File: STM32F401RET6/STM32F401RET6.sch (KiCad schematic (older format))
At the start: 12 parts

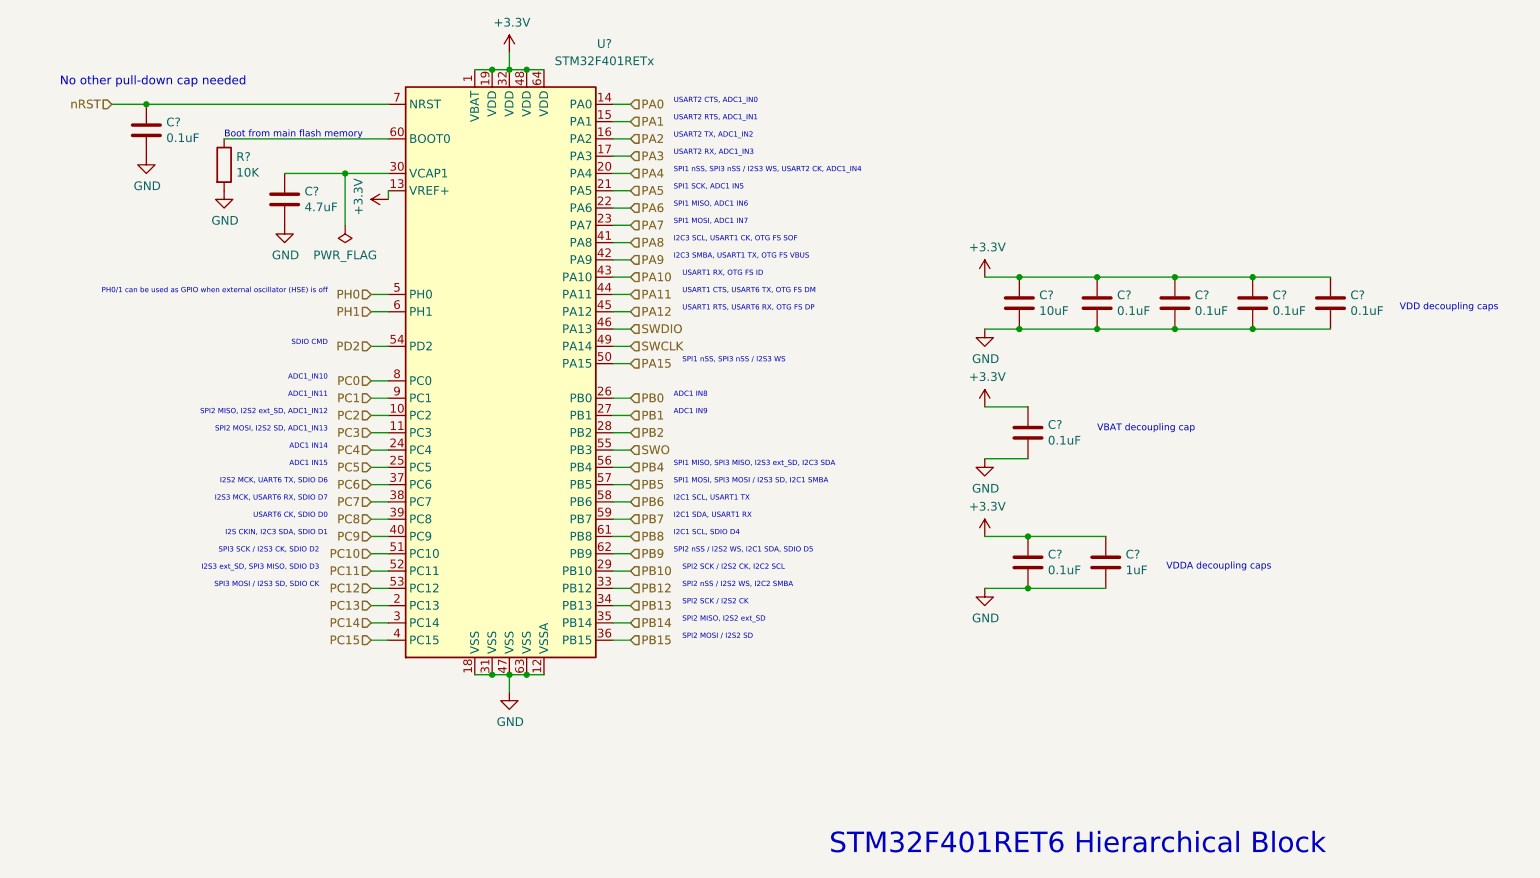
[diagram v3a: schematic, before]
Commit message: add symbol libraries, and cleanup
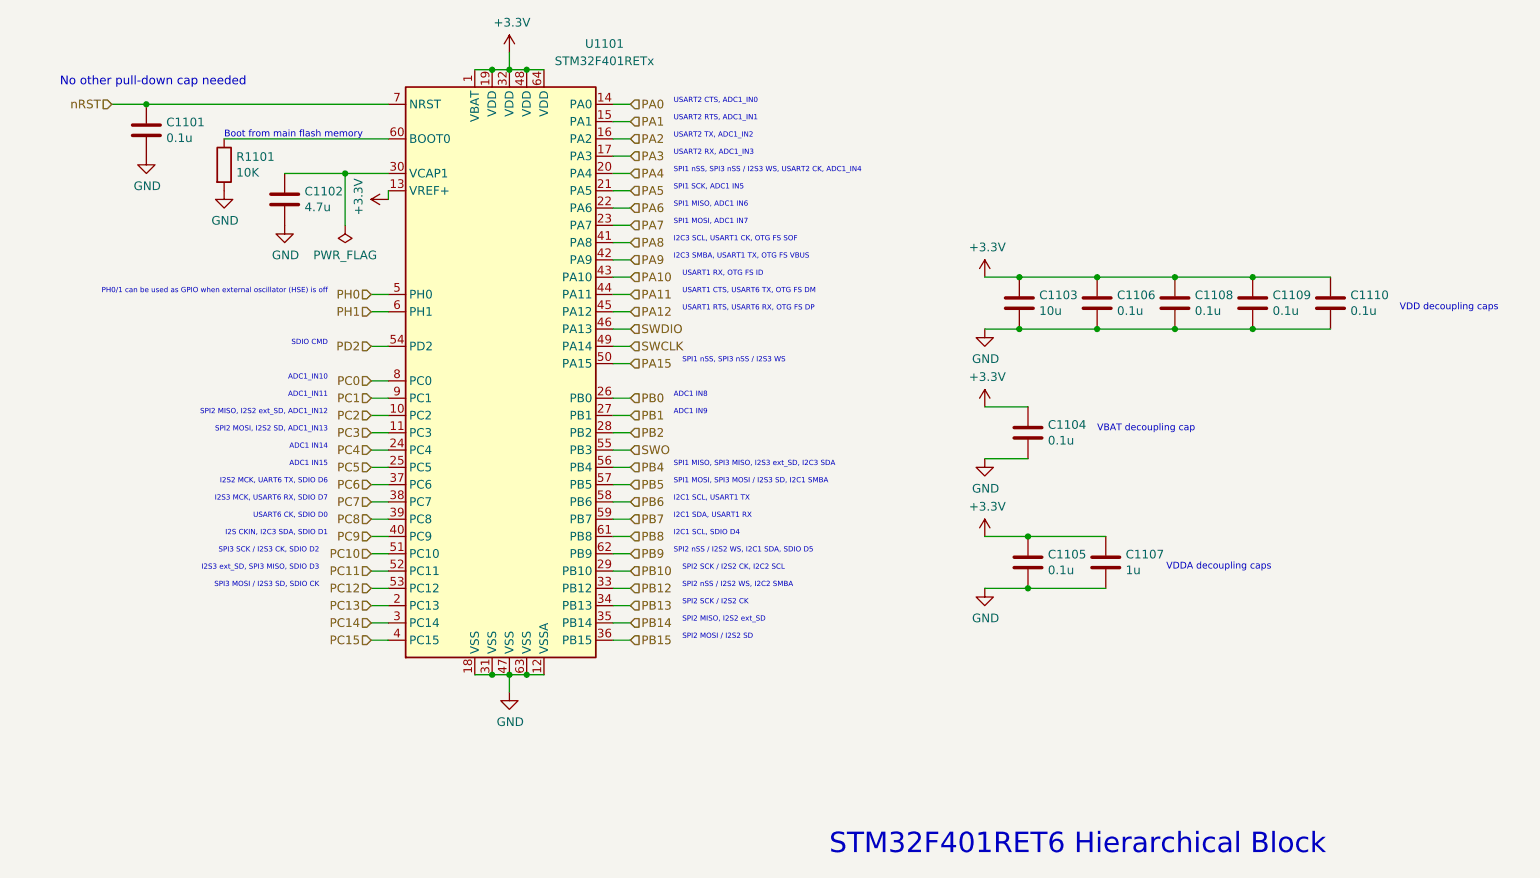
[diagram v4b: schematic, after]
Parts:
- C1101, C1104, C1105, C1106, C1108, C1109, C1110: renamed from C?; value 0.1uF -> 0.1u; footprint (none) -> Capacitor_SMD:C_0603_1608Metric; DIGIKEY (none) -> 399-1100-1-ND; MANF (none) -> C0603C104Z3VACTU
- C1102: renamed from C?; value 4.7uF -> 4.7u; footprint (none) -> Capacitor_SMD:C_0603_1608Metric; DIGIKEY (none) -> 311-1820-1-ND; MANF (none) -> CC0603MRX5R6BB475
- C1103: renamed from C?; value 10uF -> 10u; footprint (none) -> Capacitor_SMD:C_0603_1608Metric; DIGIKEY (none) -> 490-13248-1-ND; MANF (none) -> GRM188R6YA106MA73D
- C1107: renamed from C?; value 1uF -> 1u; footprint (none) -> Capacitor_SMD:C_0603_1608Metric; DIGIKEY (none) -> 1276-1182-1-ND; MANF (none) -> CL10A105KP8NNNC
- R1101: renamed from R?; footprint (none) -> Resistor_SMD:R_0603_1608Metric; DIGIKEY (none) -> 311-10KGRCT-ND; MANF (none) -> RC0603JR-0710KL
- U1101: renamed from U?; DIGIKEY (none) -> 497-17429-ND; MANF (none) -> STM32F401RET6
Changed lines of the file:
@@
 $Descr A4 11693 8268
 encoding utf-8
-Sheet 4 6
+Sheet 1 1
 Title ""
 Date ""
@@
 $EndDescr
 $Comp
-L MCU_ST_STM32F4:STM32F401RETx U?
+L MCU_ST_STM32F4:STM32F401RETx U1101
 U 1 1 5DE1731E
 P 5250 4100
-F 0 "U?" H 5800 5950 50  0000 C CNN
+F 0 "U1101" H 5800 5950 50  0000 C CNN
 F 1 "STM32F401RETx" H 5800 5850 50  0000 C CNN
 F 2 "Package_QFP:LQFP-64_10x10mm_P0.5mm" H 4650 2400 50  0001 R CNN
 F 3 "http://www.st.com/st-web-ui/static/active/en/resource/technical/document/datasheet/DM00102166.pdf" H 5250 4100 50  0001 C CNN
+F 4 "497-17429-ND" H 5250 4100 50  0001 C CNN "DIGIKEY"
+F 5 "STM32F401RET6" H 5250 4100 50  0001 C CNN "MANF"
 	1    5250 4100
 	1    0    0    -1
@@
 	5250 2300 5250 2400
 $Comp
-L power:GND #PWR?
+L power:GND #PWR01106
 U 1 1 5DE18883
 P 5250 6000
-F 0 "#PWR?" H 5250 5750 50  0001 C CNN
+F 0 "#PWR01106" H 5250 5750 50  0001 C CNN
 F 1 "GND" H 5255 5827 50  0000 C CNN
 F 2 "" H 5250 6000 50  0001 C CNN
@@
 	5250 6000 5250 5900
 $Comp
-L Device:C C?
+L Device:C C1106
 U 1 1 5DE19367
 P 8650 3750
-F 0 "C?" H 8765 3796 50  0000 L CNN
-F 1 "0.1uF" H 8765 3705 50  0000 L CNN
-F 2 "" H 8688 3600 50  0001 C CNN
+F 0 "C1106" H 8765 3796 50  0000 L CNN
+F 1 "0.1u" H 8765 3705 50  0000 L CNN
+F 2 "Capacitor_SMD:C_0603_1608Metric" H 8688 3600 50  0001 C CNN
 F 3 "~" H 8650 3750 50  0001 C CNN
+F 4 "399-1100-1-ND" H 8650 3750 50  0001 C CNN "DIGIKEY"
+F 5 "C0603C104Z3VACTU" H 8650 3750 50  0001 C CNN "MANF"
 	1    8650 3750
 	1    0    0    -1
 $EndComp
 $Comp
-L Device:C C?
+L Device:C C1108
 U 1 1 5DE19787
 P 9100 3750
-F 0 "C?" H 9215 3796 50  0000 L CNN
-F 1 "0.1uF" H 9215 3705 50  0000 L CNN
-F 2 "" H 9138 3600 50  0001 C CNN
+F 0 "C1108" H 9215 3796 50  0000 L CNN
+F 1 "0.1u" H 9215 3705 50  0000 L CNN
+F 2 "Capacitor_SMD:C_0603_1608Metric" H 9138 3600 50  0001 C CNN
 F 3 "~" H 9100 3750 50  0001 C CNN
+F 4 "399-1100-1-ND" H 9100 3750 50  0001 C CNN "DIGIKEY"
+F 5 "C0603C104Z3VACTU" H 9100 3750 50  0001 C CNN "MANF"
 	1    9100 3750
 	1    0    0    -1
 $EndComp
 $Comp
-L Device:C C?
+L Device:C C1109
 U 1 1 5DE19D37
 P 9550 3750
-F 0 "C?" H 9665 3796 50  0000 L CNN
-F 1 "0.1uF" H 9665 3705 50  0000 L CNN
-F 2 "" H 9588 3600 50  0001 C CNN
+F 0 "C1109" H 9665 3796 50  0000 L CNN
+F 1 "0.1u" H 9665 3705 50  0000 L CNN
+F 2 "Capacitor_SMD:C_0603_1608Metric" H 9588 3600 50  0001 C CNN
 F 3 "~" H 9550 3750 50  0001 C CNN
+F 4 "399-1100-1-ND" H 9550 3750 50  0001 C CNN "DIGIKEY"
+F 5 "C0603C104Z3VACTU" H 9550 3750 50  0001 C CNN "MANF"
 	1    9550 3750
 	1    0    0    -1
 $EndComp
 $Comp
-L Device:C C?
+L Device:C C1110
 U 1 1 5DE19F0D
 P 10000 3750
-F 0 "C?" H 10115 3796 50  0000 L CNN
-F 1 "0.1uF" H 10115 3705 50  0000 L CNN
-F 2 "" H 10038 3600 50  0001 C CNN
+F 0 "C1110" H 10115 3796 50  0000 L CNN
+F 1 "0.1u" H 10115 3705 50  0000 L CNN
+F 2 "Capacitor_SMD:C_0603_1608Metric" H 10038 3600 50  0001 C CNN
 F 3 "~" H 10000 3750 50  0001 C CNN
+F 4 "399-1100-1-ND" H 10000 3750 50  0001 C CNN "DIGIKEY"
+F 5 "C0603C104Z3VACTU" H 10000 3750 50  0001 C CNN "MANF"
 	1    10000 3750
 	1    0    0    -1
@@
 	8200 3900 8650 3900
 $Comp
-L Device:C C?
+L Device:C C1103
 U 1 1 5DE19136
 P 8200 3750
-F 0 "C?" H 8315 3796 50  0000 L CNN
-F 1 "10uF" H 8315 3705 50  0000 L CNN
-F 2 "" H 8238 3600 50  0001 C CNN
+F 0 "C1103" H 8315 3796 50  0000 L CNN
+F 1 "10u" H 8315 3705 50  0000 L CNN
+F 2 "Capacitor_SMD:C_0603_1608Metric" H 8238 3600 50  0001 C CNN
 F 3 "~" H 8200 3750 50  0001 C CNN
+F 4 "490-13248-1-ND" H 8200 3750 50  0001 C CNN "DIGIKEY"
+F 5 "GRM188R6YA106MA73D" H 8200 3750 50  0001 C CNN "MANF"
 	1    8200 3750
 	1    0    0    -1
 $EndComp
 $Comp
-L power:GND #PWR?
+L power:GND #PWR01108
 U 1 1 5DE18B06
 P 8000 3900
-F 0 "#PWR?" H 8000 3650 50  0001 C CNN
+F 0 "#PWR01108" H 8000 3650 50  0001 C CNN
 F 1 "GND" H 8005 3727 50  0000 C CNN
 F 2 "" H 8000 3900 50  0001 C CNN
@@
 $EndComp
 $Comp
-L power:GND #PWR?
+L power:GND #PWR01110
 U 1 1 5DE1D921
 P 8000 4650
-F 0 "#PWR?" H 8000 4400 50  0001 C CNN
+F 0 "#PWR01110" H 8000 4400 50  0001 C CNN
 F 1 "GND" H 8005 4477 50  0000 C CNN
 F 2 "" H 8000 4650 50  0001 C CNN
@@
 $EndComp
 $Comp
-L Device:C C?
+L Device:C C1104
 U 1 1 5DE1DB7A
 P 8250 4500
-F 0 "C?" H 8365 4546 50  0000 L CNN
-F 1 "0.1uF" H 8365 4455 50  0000 L CNN
-F 2 "" H 8288 4350 50  0001 C CNN
+F 0 "C1104" H 8365 4546 50  0000 L CNN
+F 1 "0.1u" H 8365 4455 50  0000 L CNN
+F 2 "Capacitor_SMD:C_0603_1608Metric" H 8288 4350 50  0001 C CNN
 F 3 "~" H 8250 4500 50  0001 C CNN
+F 4 "399-1100-1-ND" H 8250 4500 50  0001 C CNN "DIGIKEY"
+F 5 "C0603C104Z3VACTU" H 8250 4500 50  0001 C CNN "MANF"
 	1    8250 4500
 	1    0    0    -1
@@
 	8250 4350 8000 4350
 $Comp
-L Device:C C?
+L Device:C C1105
 U 1 1 5DE1EBB5
 P 8250 5250
-F 0 "C?" H 8365 5296 50  0000 L CNN
-F 1 "0.1uF" H 8365 5205 50  0000 L CNN
-F 2 "" H 8288 5100 50  0001 C CNN
+F 0 "C1105" H 8365 5296 50  0000 L CNN
+F 1 "0.1u" H 8365 5205 50  0000 L CNN
+F 2 "Capacitor_SMD:C_0603_1608Metric" H 8288 5100 50  0001 C CNN
 F 3 "~" H 8250 5250 50  0001 C CNN
+F 4 "399-1100-1-ND" H 8250 5250 50  0001 C CNN "DIGIKEY"
+F 5 "C0603C104Z3VACTU" H 8250 5250 50  0001 C CNN "MANF"
 	1    8250 5250
 	1    0    0    -1
 $EndComp
 $Comp
-L power:GND #PWR?
+L power:GND #PWR01112
 U 1 1 5DE1F4FA
 P 8000 5400
-F 0 "#PWR?" H 8000 5150 50  0001 C CNN
+F 0 "#PWR01112" H 8000 5150 50  0001 C CNN
 F 1 "GND" H 8005 5227 50  0000 C CNN
 F 2 "" H 8000 5400 50  0001 C CNN
@@
 $EndComp
 $Comp
-L Device:C C?
+L Device:C C1107
 U 1 1 5DE17F46
 P 8700 5250
-F 0 "C?" H 8815 5296 50  0000 L CNN
-F 1 "1uF" H 8815 5205 50  0000 L CNN
-F 2 "" H 8738 5100 50  0001 C CNN
+F 0 "C1107" H 8815 5296 50  0000 L CNN
+F 1 "1u" H 8815 5205 50  0000 L CNN
+F 2 "Capacitor_SMD:C_0603_1608Metric" H 8738 5100 50  0001 C CNN
 F 3 "~" H 8700 5250 50  0001 C CNN
+F 4 "1276-1182-1-ND" H 8700 5250 50  0001 C CNN "DIGIKEY"
+F 5 "CL10A105KP8NNNC" H 8700 5250 50  0001 C CNN "MANF"
 	1    8700 5250
 	1    0    0    -1
@@
 VDD decoupling caps
 $Comp
-L Device:C C?
+L Device:C C1102
 U 1 1 5DE1ABC6
 P 3950 3150
-F 0 "C?" H 4065 3196 50  0000 L CNN
-F 1 "4.7uF" H 4065 3105 50  0000 L CNN
-F 2 "" H 3988 3000 50  0001 C CNN
+F 0 "C1102" H 4065 3196 50  0000 L CNN
+F 1 "4.7u" H 4065 3105 50  0000 L CNN
+F 2 "Capacitor_SMD:C_0603_1608Metric" H 3988 3000 50  0001 C CNN
 F 3 "~" H 3950 3150 50  0001 C CNN
+F 4 "311-1820-1-ND" H 3950 3150 50  0001 C CNN "DIGIKEY"
+F 5 "CC0603MRX5R6BB475" H 3950 3150 50  0001 C CNN "MANF"
 	1    3950 3150
 	1    0    0    -1
 $EndComp
 $Comp
-L power:GND #PWR?
+L power:GND #PWR01103
 U 1 1 5DE1B283
 P 3950 3300
-F 0 "#PWR?" H 3950 3050 50  0001 C CNN
+F 0 "#PWR01103" H 3950 3050 50  0001 C CNN
 F 1 "GND" H 3955 3127 50  0000 C CNN
 F 2 "" H 3950 3300 50  0001 C CNN
@@
 	3950 3000 4300 3000
 $Comp
-L Device:C C?
+L Device:C C1101
 U 1 1 5DE1BE22
 P 3150 2750
-F 0 "C?" H 3265 2796 50  0000 L CNN
-F 1 "0.1uF" H 3265 2705 50  0000 L CNN
-F 2 "" H 3188 2600 50  0001 C CNN
+F 0 "C1101" H 3265 2796 50  0000 L CNN
+F 1 "0.1u" H 3265 2705 50  0000 L CNN
+F 2 "Capacitor_SMD:C_0603_1608Metric" H 3188 2600 50  0001 C CNN
 F 3 "~" H 3150 2750 50  0001 C CNN
+F 4 "399-1100-1-ND" H 3150 2750 50  0001 C CNN "DIGIKEY"
+F 5 "C0603C104Z3VACTU" H 3150 2750 50  0001 C CNN "MANF"
 	1    3150 2750
 	1    0    0    -1
@@
 	2950 2600 3150 2600
 $Comp
-L power:GND #PWR?
+L power:GND #PWR01101
 U 1 1 5DE1D367
 P 3150 2900
-F 0 "#PWR?" H 3150 2650 50  0001 C CNN
+F 0 "#PWR01101" H 3150 2650 50  0001 C CNN
 F 1 "GND" H 3155 2727 50  0000 C CNN
 F 2 "" H 3150 2900 50  0001 C CNN
@@
 Connection ~ 3150 2600
 $Comp
-L Device:R R?
+L Device:R R1101
 U 1 1 5DE1E2D2
 P 3600 2950
-F 0 "R?" H 3670 2996 50  0000 L CNN
+F 0 "R1101" H 3670 2996 50  0000 L CNN
 F 1 "10K" H 3670 2905 50  0000 L CNN
-F 2 "" V 3530 2950 50  0001 C CNN
+F 2 "Resistor_SMD:R_0603_1608Metric" V 3530 2950 50  0001 C CNN
 F 3 "~" H 3600 2950 50  0001 C CNN
+F 4 "311-10KGRCT-ND" H 3600 2950 50  0001 C CNN "DIGIKEY"
+F 5 "RC0603JR-0710KL" H 3600 2950 50  0001 C CNN "MANF"
 	1    3600 2950
 	1    0    0    -1
 $EndComp
 $Comp
-L power:GND #PWR?
+L power:GND #PWR01102
 U 1 1 5DE1E857
 P 3600 3100
-F 0 "#PWR?" H 3600 2850 50  0001 C CNN
+F 0 "#PWR01102" H 3600 2850 50  0001 C CNN
 F 1 "GND" H 3605 2927 50  0000 C CNN
 F 2 "" H 3600 3100 50  0001 C CNN
@@
 SPI2 nSS / I2S2 WS, I2C1 SDA, SDIO D5
 $Comp
-L power:+3.3V #PWR?
+L power:+3.3V #PWR01105
 U 1 1 5DE1F0DC
 P 5250 2300
-F 0 "#PWR?" H 5250 2150 50  0001 C CNN
+F 0 "#PWR01105" H 5250 2150 50  0001 C CNN
 F 1 "+3.3V" H 5265 2473 50  0000 C CNN
 F 2 "" H 5250 2300 50  0001 C CNN
@@
 $EndComp
 $Comp
-L power:+3.3V #PWR?
+L power:+3.3V #PWR01107
 U 1 1 5DE22E45
 P 8000 3600
-F 0 "#PWR?" H 8000 3450 50  0001 C CNN
+F 0 "#PWR01107" H 8000 3450 50  0001 C CNN
 F 1 "+3.3V" H 8015 3773 50  0000 C CNN
 F 2 "" H 8000 3600 50  0001 C CNN
@@
 $EndComp
 $Comp
-L power:+3.3V #PWR?
+L power:+3.3V #PWR01109
 U 1 1 5DE235AC
 P 8000 4350
-F 0 "#PWR?" H 8000 4200 50  0001 C CNN
+F 0 "#PWR01109" H 8000 4200 50  0001 C CNN
 F 1 "+3.3V" H 8015 4523 50  0000 C CNN
 F 2 "" H 8000 4350 50  0001 C CNN
@@
 $EndComp
 $Comp
-L power:+3.3V #PWR?
+L power:+3.3V #PWR01111
 U 1 1 5DE2397A
 P 8000 5100
-F 0 "#PWR?" H 8000 4950 50  0001 C CNN
+F 0 "#PWR01111" H 8000 4950 50  0001 C CNN
 F 1 "+3.3V" H 8015 5273 50  0000 C CNN
 F 2 "" H 8000 5100 50  0001 C CNN
@@
 STM32F401RET6 Hierarchical Block
 $Comp
-L power:+3.3V #PWR?
+L power:+3.3V #PWR01104
 U 1 1 5DE2F79B
 P 4550 3150
-F 0 "#PWR?" H 4550 3000 50  0001 C CNN
+F 0 "#PWR01104" H 4550 3000 50  0001 C CNN
 F 1 "+3.3V" H 4565 3323 50  0000 C CNN
 F 2 "" H 4550 3150 50  0001 C CNN
@@
 	4550 3100 4550 3150
 $Comp
-L power:PWR_FLAG #FLG?
+L power:PWR_FLAG #FLG01101
 U 1 1 5DE3436C
 P 4300 3300
-F 0 "#FLG?" H 4300 3375 50  0001 C CNN
+F 0 "#FLG01101" H 4300 3375 50  0001 C CNN
 F 1 "PWR_FLAG" H 4300 3473 50  0000 C CNN
 F 2 "" H 4300 3300 50  0001 C CNN
